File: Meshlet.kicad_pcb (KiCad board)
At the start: 2 copper layers, 60.2 x 39 mm, 98 parts, among them J1 Ext. Notif. Header, J10 STEMMA QT I2C, J11 GPIO Exp., J12 I2C PINHEADER, J2 USB_C_Receptacle_USB2.0_16P, J3 Ext. Power Header, J4 Batt. Header (JST-PH 2.0), J5 SWD, J6 Batt. Header (Picoblade 1.25), J7 GPS Header, J8 User Btn Header, J9 Power Switch, Q1 AO3400A, SW1 BOOTSEL, SW3 RST, U1 W25Q32JVZP, U2 XC6206PxxxMR, U3 RP2350_60QFN, U4 INA3221, U5 BME280, U6 Wio-SX1262, U7 USBLC6-2SC6, U8 BQ24074RGT, Y1 12.000MHz

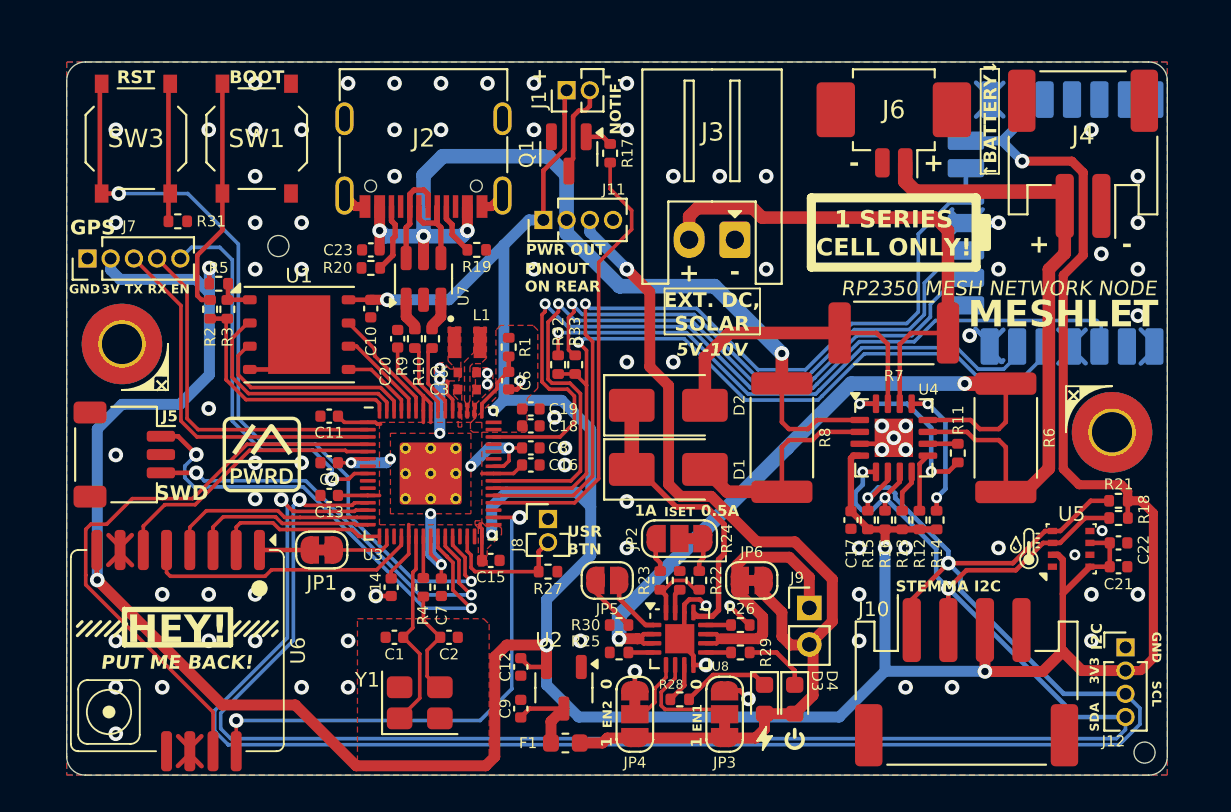
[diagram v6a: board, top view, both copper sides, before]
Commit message: Fixed several design flaws. More caps, more LDOs, etc
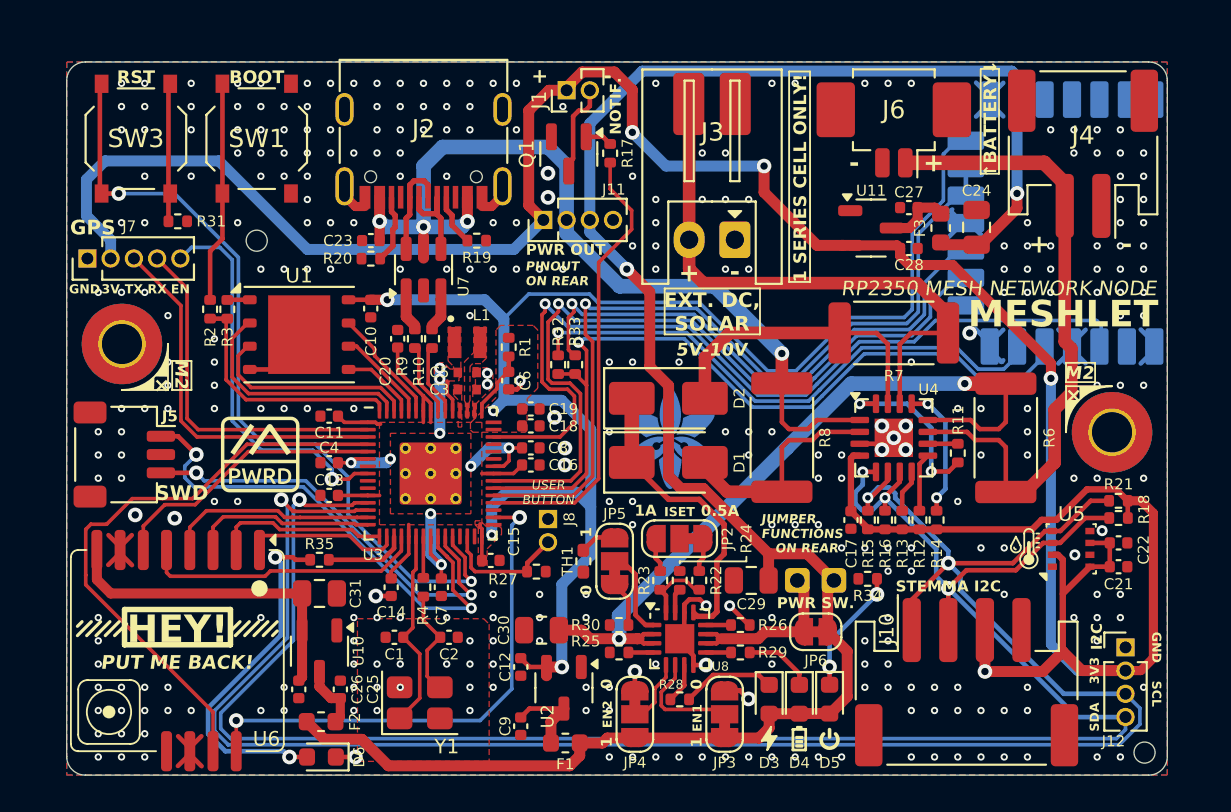
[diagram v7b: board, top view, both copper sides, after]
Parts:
- removed JP1: RF_SW Jumper, Jumper:SolderJumper-2_P1.3mm_Bridged_RoundedPad1.0x1.5mm
- removed R5: DNF, Resistor_SMD:R_0402_1005Metric
- added C24: 47uF, Capacitor_SMD:C_0805_2012Metric, F.Cu at (160.0, 63.2)
- added C25: 1uF, Capacitor_SMD:C_0402_1005Metric, F.Cu at (125.2, 88.5)
- added C26: 1uF, Capacitor_SMD:C_0402_1005Metric, F.Cu at (122.9, 88.5)
- added C27: 1uF, Capacitor_SMD:C_0402_1005Metric, F.Cu at (156.3, 62.1)
- added C28: 1uF, Capacitor_SMD:C_0402_1005Metric, F.Cu at (156.3, 64.4)
- added C29: 47uF, Capacitor_SMD:C_0805_2012Metric, F.Cu at (147.7, 82.5)
- added C30: 47uF, Capacitor_SMD:C_0805_2012Metric, F.Cu at (136.2, 85.2)
- added C31: 47uF, Capacitor_SMD:C_0805_2012Metric, F.Cu at (124.1, 83.2)
- added D5: PWR, LED_SMD:LED_0603_1608Metric, F.Cu at (152.0, 89.0)
- added D6: HB, LED_SMD:LED_0603_1608Metric, F.Cu at (124.2, 92.2)
- added F2: 6V 0.5A, Fuse:Fuse_0603_1608Metric, F.Cu at (124.2, 90.2)
- added F3: 6V 0.5A, Fuse:Fuse_0603_1608Metric, F.Cu at (158.0, 63.3)
- added J13: Ext. Power Header, Connector_PinHeader_2.54mm:PinHeader_1x02_P2.54mm_Vertical, F.Cu at (146.8, 56.5)
- added R34: 10k, Resistor_SMD:R_0402_1005Metric, F.Cu at (154.1, 82.4)
- added R35: 10k, Resistor_SMD:R_0402_1005Metric, F.Cu at (124.1, 81.4)
- added TH1: Thermistor_NTC, Resistor_SMD:R_0402_1005Metric_Pad0.72x0.64mm_HandSolder, F.Cu at (138.5, 81.5)
- added U10: XC6206PxxxMR, Package_TO_SOT_SMD:SOT-23-3, F.Cu at (124.1, 86.4)
- added U11: XC6206PxxxMR, Package_TO_SOT_SMD:SOT-23-3, F.Cu at (154.2, 63.3)
- D3: value GRN -> PG
- D4: value RED -> CHG
- JP5: value BMS TS Jumper -> Jumper_3_Bridged12; footprint Jumper:SolderJumper-2_P1.3mm_Open_RoundedPad1.0x1.5mm -> Jumper:SolderJumper-3_P1.3mm_Bridged12_RoundedPad1.0x1.5mm
- R30: value 10k Thermistor -> 10k
- R6, R7, R8: value PT2512FK-070R1L -> PA2512FKF7W0R01E
- moved JP6 4.49 mm to (151.2, 85.3)
- moved J9 1.64 mm to (150.2, 82.5), turned to 90 degrees
- moved REF** 1.22 mm to (120.7, 64.0)
- moved JP5 1.13 mm to (140.2, 81.5), turned to 90 degrees
- moved C9 0.96 mm to (135.1, 90.5), turned to -90 degrees
- moved R27 0.63 mm to (135.9, 82.0)
- moved C23 0.51 mm to (126.9, 63.9)
- moved R19 0.51 mm to (132.7, 63.9)
- moved R20 0.51 mm to (126.9, 64.9)
- moved U7 0.51 mm to (129.8, 65.5)
- moved J2 0.51 mm to (129.8, 57.9)
- moved D1 0.38 mm to (143.2, 76.1)
- moved D2 0.38 mm to (143.2, 72.6)
- moved D3 0.25 mm to (148.7, 89.0)
- moved D4 0.25 mm to (150.3, 89.0)
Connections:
- C10 pad 1: +3V3 -> /Pi +3V3
- C11 pad 1: +3V3 -> /Pi +3V3
- C12 pad 1: +3V3 -> /Pi +3V3
- C13 pad 1: +3V3 -> /Pi +3V3
- C14 pad 1: +3V3 -> /Pi +3V3
- C15 pad 1: +3V3 -> /Pi +3V3
- C16 pad 1: +3V3 -> /Pi +3V3
- C18 pad 1: +3V3 -> /Pi +3V3
- C19 pad 1: +3V3 -> /Pi +3V3
- C20 pad 1: +3V3 -> /Pi +3V3
- C3 pad 1: +3V3 -> /Pi +3V3
- JP5 pad 2: Net-(JP5-B) -> Net-(JP5-C)
- R1 pad 1: +3V3 -> /Pi +3V3
- R30 pad 1: Net-(JP5-B) -> Net-(JP5-A)
- U1 pad 8: +3V3 -> /Pi +3V3
- U2 pad 2: +3V3 -> /Pi +3V3
- U3 pad 1: +3V3 -> /Pi +3V3
- U3 pad 11: +3V3 -> /Pi +3V3
- U3 pad 17: Net-(JP1-A) -> LORA_RF_SW
- U3 pad 18: unconnected-(U3-GPIO14-Pad18) -> Net-(U3-GPIO14)
- U3 pad 20: +3V3 -> /Pi +3V3
- U3 pad 30: +3V3 -> /Pi +3V3
- U3 pad 38: +3V3 -> /Pi +3V3
- U3 pad 44: +3V3 -> /Pi +3V3
- U3 pad 45: +3V3 -> /Pi +3V3
- U3 pad 49: +3V3 -> /Pi +3V3
- U3 pad 53: +3V3 -> /Pi +3V3
- U3 pad 54: +3V3 -> /Pi +3V3
- U6 pad 8: +3V3 -> /LoRa +3V3
- U8 pad 1: Net-(JP5-A) -> Net-(JP5-C)
- U9 pad 14: +3V3 -> /Pi +3V3
- U9 pad 16: +3V3 -> BMS_OUT
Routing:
- net +3V3: track 255.4 -> 155.0 mm, vias 9 -> 4
- net /Pi +3V3: track 0.00 -> 99.3 mm, vias 0 -> 4
- net BMS_OUT: track 53.9 -> 110.8 mm, vias 1 -> 2
- net Net-(D6-A): track 0.00 -> 19.3 mm, vias 0 -> 2
- net /LoRa +3V3: track 0.00 -> 18.0 mm
- net Net-(D5-K): track 0.00 -> 6.86 mm, vias 0 -> 2
- net LORA_RF_SW: track 2.76 -> 8.63 mm
- net Net-(J9-Pin_1): track 14.9 -> 9.49 mm
- net Net-(JP5-C): track 0.00 -> 4.87 mm
- net Net-(U3-GPIO14): track 0.00 -> 4.48 mm
- net Net-(U11-VI): track 0.00 -> 3.66 mm
- net Net-(U10-VI): track 0.00 -> 3.60 mm
- net INA_IN2-: track 27.9 -> 31.4 mm
- net Net-(JP1-A): track 3.49 -> 0.00 mm
- net INA_IN1+: track 37.3 -> 40.8 mm
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- added copper zone on F.Cu, net /Pi +3V3
- removed copper zone on F.Cu, net +3V3
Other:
- board text added: "DESIGNED IN"
- board text added: "EDMONTON, AB"
- board text added: "EP V0.2"
- board text added: "MESH NETWORK NODE RP2350 MESH NETWORK NODE RP2350"
- board text added: "ON REAR"
- board text added: "PWR SW."
- board text added: "RPI RM2"
- board text added: "Thermistor (cut & jump to 1 if present)"
- board text added: "USER BUTTON"
- board text added: "VERSION 0.2"
- board text removed: "10K Thermistor (default disconnected)"
- board text removed: "JP6:"
- board text removed: "POWER SWITCH"
- board text removed: "RF_SW Pin Adjustment (just in case)"
- board text removed: "RP2350 MESH NETWORK NODE RP2350 MESH NETWORK NODE"
- board text removed: "USR BTN"
- board text removed: "V0.1"
- board text removed: "VERSION 0.1"
